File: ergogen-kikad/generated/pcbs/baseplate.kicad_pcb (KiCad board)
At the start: 2 copper layers, 114.2 x 55 mm, 22 parts, among them J1 Header clearance

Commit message: Move outer M2 mounts between fifth keys and controls
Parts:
- moved H5 28.5 mm to (256.4, 129.8)
- moved H6 28.5 mm to (256.4, 167.2)

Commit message: Recess original battery through main PCB onto intact baseplate
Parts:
- BAT1: value 301055 220mAh max 57.5x10.5x3.5 -> 301055 220mAh max 57.5x10.5x3.5 z=-1.4
- moved BAT1 0.75 mm to (183.3, 148.5)

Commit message: Shift outer screws left to clear control housings
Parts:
- moved H5 1.00 mm to (255.4, 129.8)
- moved H6 1.00 mm to (255.4, 167.2)

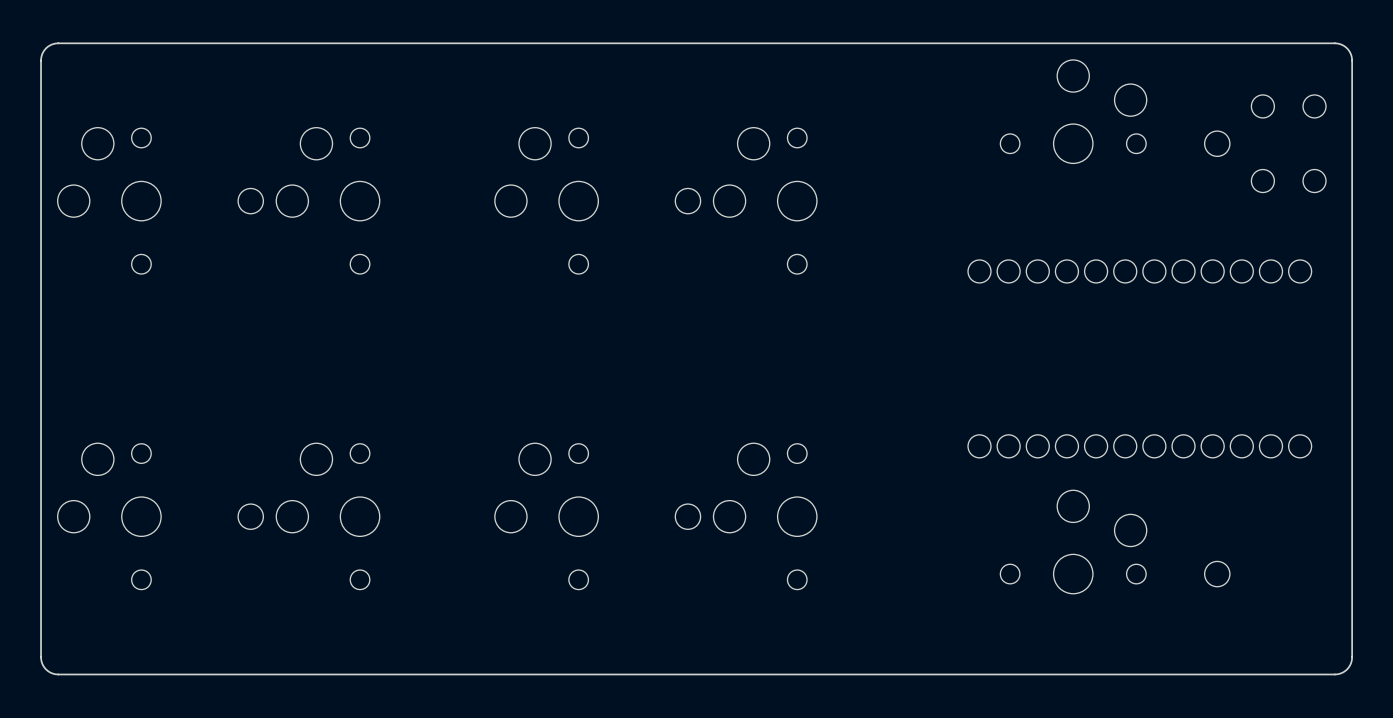
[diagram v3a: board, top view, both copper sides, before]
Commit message: Add PCB border for top-mounted case and move outer screws inward
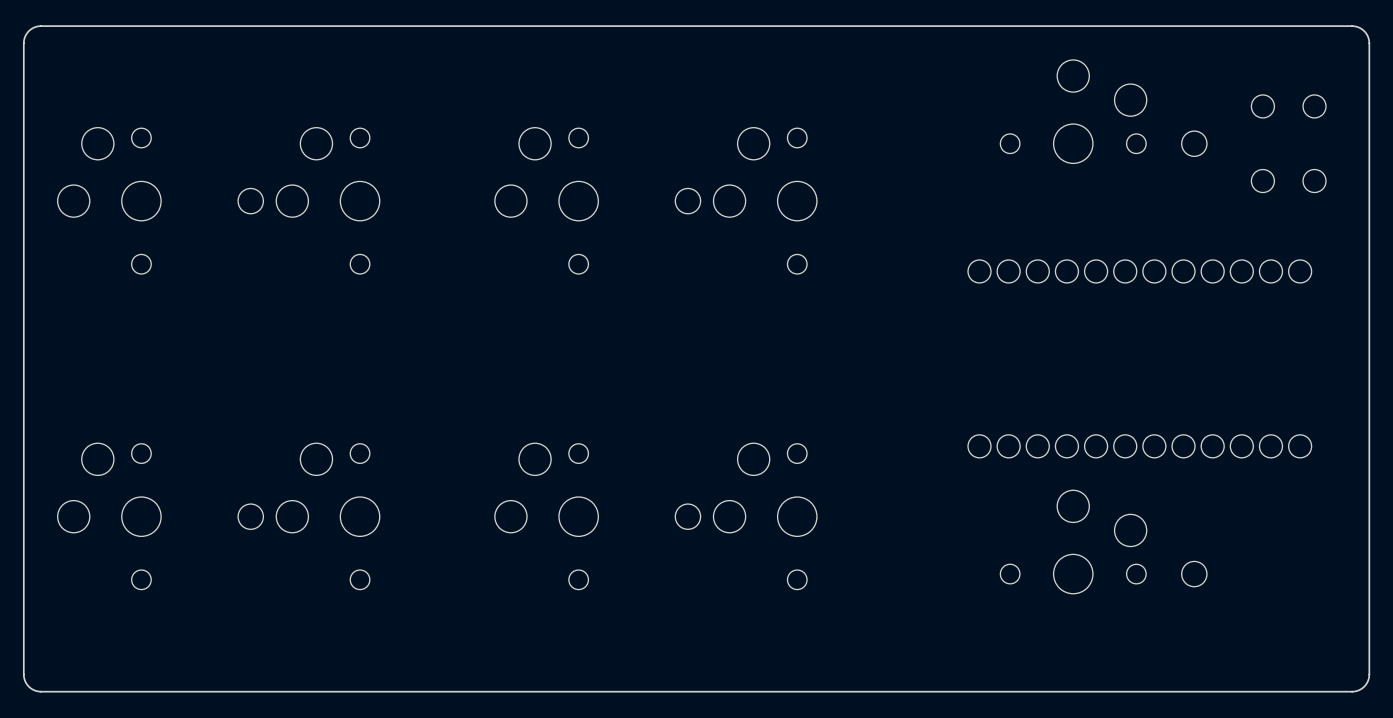
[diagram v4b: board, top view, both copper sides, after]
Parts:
- moved H5 2.00 mm to (253.4, 129.8)
- moved H6 2.00 mm to (253.4, 167.2)
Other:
- board size 114.2 x 55 mm -> 117.2 x 58 mm

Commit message: Route XIAO Plus board with recessed mounting and RF clearance
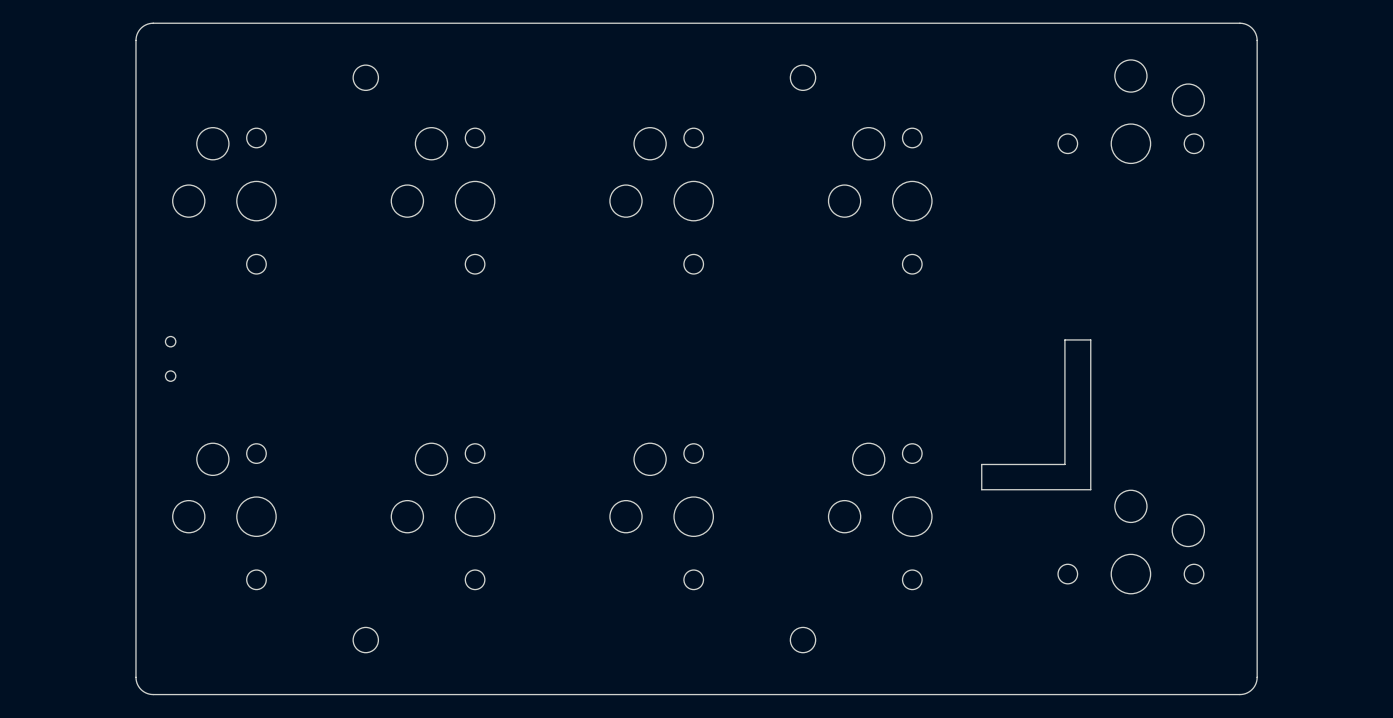
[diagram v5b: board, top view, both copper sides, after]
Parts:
- removed BAT1: 301055 220mAh max 57.5x10.5x3.5 z=-1.4, Protected_301055_Battery_Envelope
- removed H5, H6: M2 mount, M2_Mount
- removed J1, LCD1: Header clearance, 
- removed MCU1: nice!nano v2, Nice_Nano_V2
- removed RST1: 6mm top-actuated tactile, SW_PUSH_6mm_H4_3mm
- H1, H2, H3, H4: value M2 mount -> (none); footprint M2_Mount -> (none)
- PWR1: value Header clearance -> (none)
- S1, S10, S2, S3, S4, S5, S6, S7, S8, S9: value Choc v1 1.5U -> (none); footprint PG1350_1_5U -> (none)
- moved H1 14.7 mm to (181.2, 124.0)
- moved H2 14.7 mm to (219.3, 124.0)
- moved H3 14.7 mm to (181.2, 173.0)
- moved H4 14.7 mm to (219.3, 173.0)
- moved PWR1 14.0 mm to (164.5, 148.5)
- moved S1 10.0 mm to (171.7, 134.8), turned to 0 degrees
- moved S3 10.0 mm to (209.8, 134.8), turned to 0 degrees
- moved S4 10.0 mm to (228.8, 134.8), turned to 0 degrees
- moved S5 10.0 mm to (171.7, 162.2), turned to 0 degrees
- moved S7 10.0 mm to (209.8, 162.2), turned to 0 degrees
- moved S8 10.0 mm to (228.8, 162.2), turned to 0 degrees
- moved S2 10.0 mm to (190.7, 134.8), turned to 0 degrees
- moved S6 10.0 mm to (190.7, 162.2), turned to 0 degrees
- moved S10 5.03 mm to (247.8, 167.2)
- moved S9 5.03 mm to (247.8, 129.8)
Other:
- board size 117.2 x 58 mm -> 97.7 x 58.5 mm
- rule pad_to_mask_clearance: 0.05 -> 0
